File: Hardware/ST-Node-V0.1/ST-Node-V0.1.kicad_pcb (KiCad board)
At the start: 2 copper layers, 40.9 x 67.7 mm, 149 parts, among them J1 U.FL-R-SMT-1, Q1 SI2323DS, Q2 2SC4213, SW1 RESET, SW2 SW_Push, U1 TPS22917DBV, U10 LIS2DH12, U11 SHTC3, U12 ATECC608A-TNGLORAU, U2 RP605Z283B, U3 TPS22917DBV, U4 TPS22917DBV, U5 STM32WLxx_QFN48, U6 NX3L1T3157GM, U7 BGS13S4N9, U8 NX3L1T3157GM, U9 MX25R1635, X1 32MHz, X2 32.768KHz

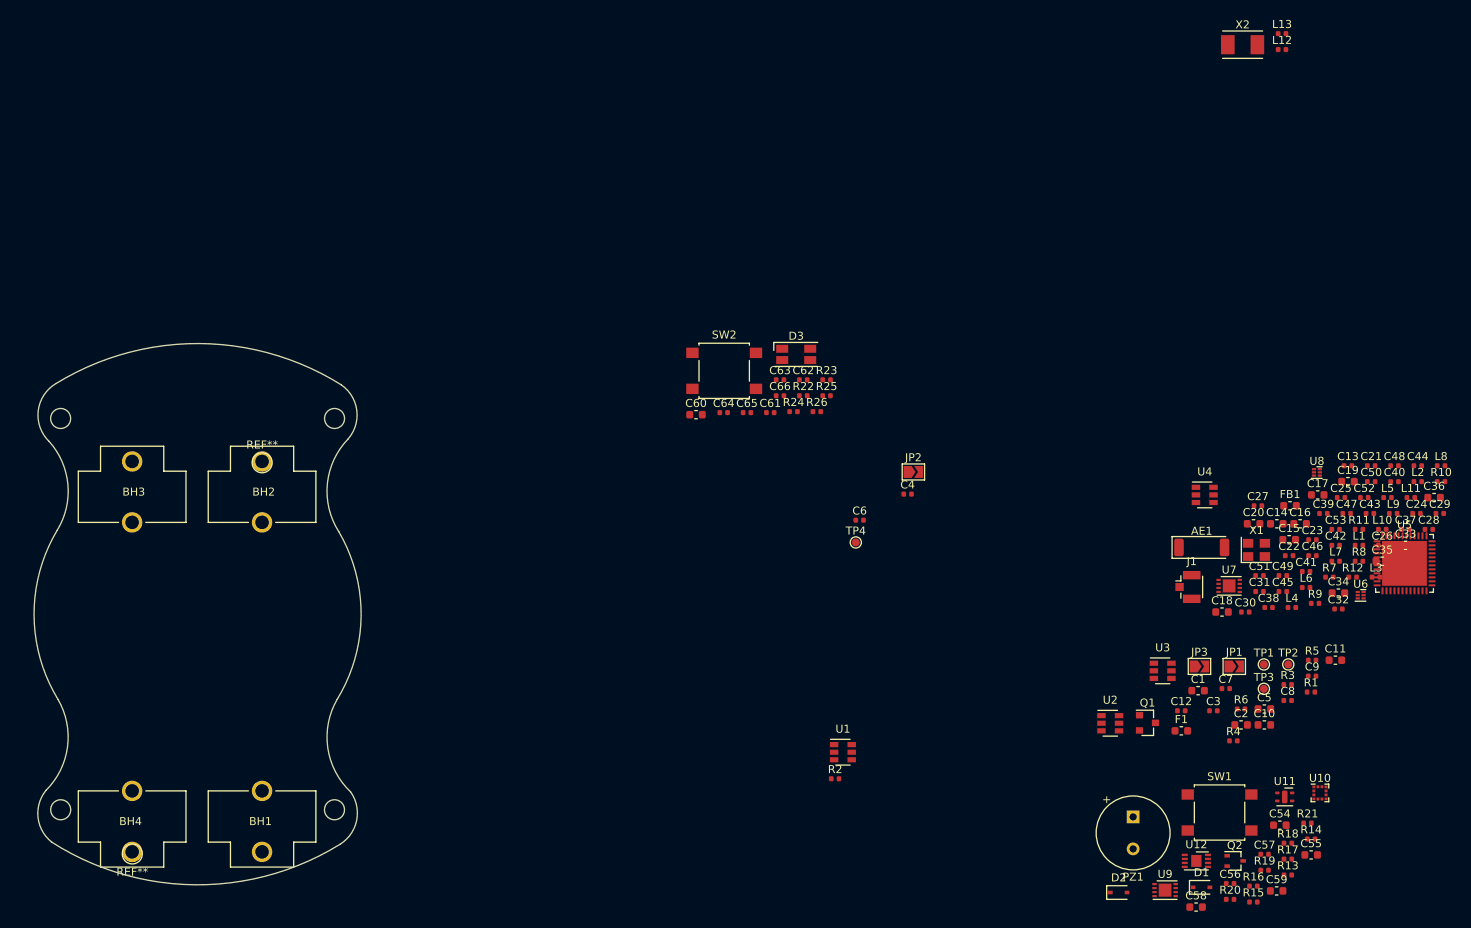
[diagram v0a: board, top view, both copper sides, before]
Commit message: sch:  Swap couple of pins and fix a HW bug
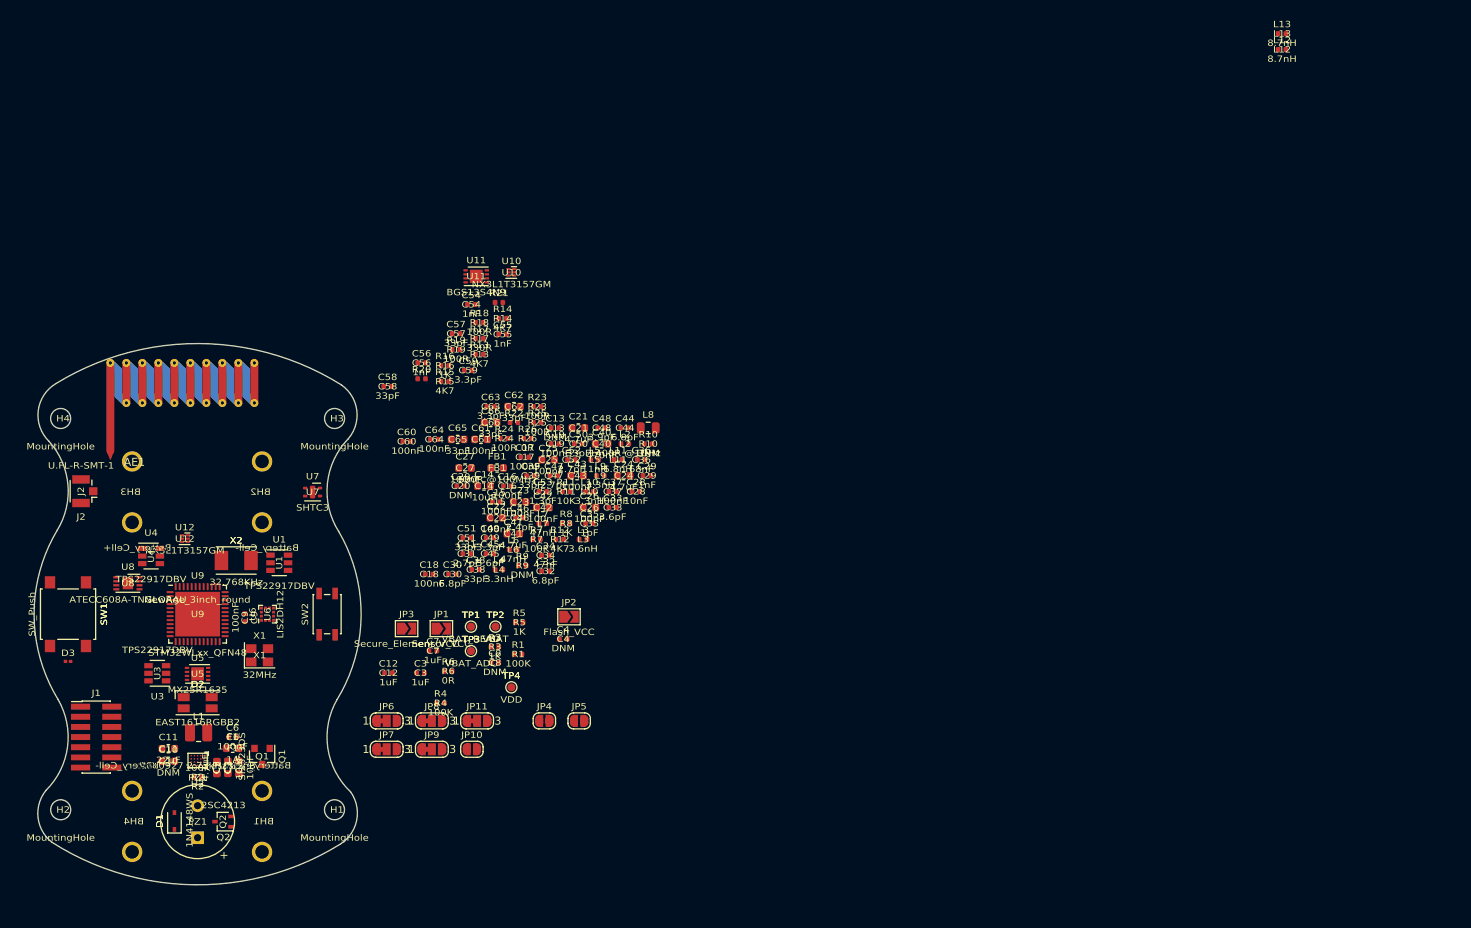
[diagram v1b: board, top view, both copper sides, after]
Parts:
- removed REF** (x2): Pin_D1.0mm_L10.0mm, Connector_Pin:Pin_D1.0mm_L10.0mm
- added J2: U.FL-R-SMT-1, Connector_Coaxial:U.FL_Hirose_U.FL-R-SMT-1_Vertical, F.Cu at (125.6, 83.7)
- added JP10: BOOT0, Jumper:SolderJumper-2_P1.3mm_Open_RoundedPad1.0x1.5mm, F.Cu at (174.0, 116.0)
- added JP11: VDD_RF_SW, Jumper:SolderJumper-3_P1.3mm_Bridged12_RoundedPad1.0x1.5mm_NumberLabels, F.Cu at (174.6, 112.4)
- added JP4: SDA, Jumper:SolderJumper-2_P1.3mm_Open_RoundedPad1.0x1.5mm, F.Cu at (183.0, 112.4)
- added JP5: SCL, Jumper:SolderJumper-2_P1.3mm_Open_RoundedPad1.0x1.5mm, F.Cu at (187.4, 112.4)
- added JP6: JTDI, Jumper:SolderJumper-3_P1.3mm_Bridged12_RoundedPad1.0x1.5mm_NumberLabels, F.Cu at (163.3, 112.4)
- added JP7: VBAT, Jumper:SolderJumper-3_P1.3mm_Bridged12_RoundedPad1.0x1.5mm_NumberLabels, F.Cu at (163.3, 116.0)
- added JP8: SWO, Jumper:SolderJumper-3_P1.3mm_Bridged12_RoundedPad1.0x1.5mm_NumberLabels, F.Cu at (169.0, 112.4)
- added JP9: PB12, Jumper:SolderJumper-3_P1.3mm_Bridged12_RoundedPad1.0x1.5mm_NumberLabels, F.Cu at (169.0, 116.0)
- AE1: value Dual_Band_868/915 -> Antenna; footprint RF_Antenna:Johanson_2450AT43F0100 -> RF_Antenna:Texas_SWRA416_868MHz_915MHz
- BH1, BH2, BH3, BH4: moved to B.Cu
- C14: value 4.7uF -> 10uF
- C15, C16, C18, C19, C58: footprint Capacitor_SMD:C_0603_1608Metric -> Capacitor_SMD:C_0402_1005Metric
- C17: value 4.7uF -> 100nF; footprint Capacitor_SMD:C_0603_1608Metric -> Capacitor_SMD:C_0402_1005Metric
- C20: value 100nF -> DNM; footprint Capacitor_SMD:C_0603_1608Metric -> Capacitor_SMD:C_0402_1005Metric
- C21: value 10nF -> 4.7uF; footprint Capacitor_SMD:C_0402_1005Metric -> Capacitor_SMD:C_0603_1608Metric
- C22: value 1nF -> 100nF; footprint Capacitor_SMD:C_0402_1005Metric -> Capacitor_SMD:C_0603_1608Metric
- C23, C25: value 6.8pF -> 100nF; footprint Capacitor_SMD:C_0402_1005Metric -> Capacitor_SMD:C_0603_1608Metric
- C24: value 2.7pF -> 4.7uF; footprint Capacitor_SMD:C_0402_1005Metric -> Capacitor_SMD:C_0603_1608Metric
- C26: value 3.6pF -> 100nF; footprint Capacitor_SMD:C_0402_1005Metric -> Capacitor_SMD:C_0603_1608Metric
- C27: value 47nF -> 100nF; footprint Capacitor_SMD:C_0402_1005Metric -> Capacitor_SMD:C_0603_1608Metric
- C28: value 1pF -> 10nF
- C29: value 68nF -> 1nF
- C30: value 100nF -> 6.8pF
- C31: value 33pF -> 2.7pF
- C32, C44: value 33pF -> 6.8pF
- C33: value 470nF -> 3.6pF; footprint Capacitor_SMD:C_0603_1608Metric -> Capacitor_SMD:C_0402_1005Metric
- C34: value 4.7uF -> 47nF; footprint Capacitor_SMD:C_0603_1608Metric -> Capacitor_SMD:C_0402_1005Metric
- C35: value 100nF -> 1pF; footprint Capacitor_SMD:C_0603_1608Metric -> Capacitor_SMD:C_0402_1005Metric
- C36: value 100nF -> 68nF; footprint Capacitor_SMD:C_0603_1608Metric -> Capacitor_SMD:C_0402_1005Metric
- C37: value 6.8pF -> 100nF
- C38: value 5.6pF -> 33pF
- C39: value 2.4pF -> 33pF
- C40: value 2.7pF -> 470nF; footprint Capacitor_SMD:C_0402_1005Metric -> Capacitor_SMD:C_0603_1608Metric
- C41: value 3.9pF -> 4.7uF; footprint Capacitor_SMD:C_0402_1005Metric -> Capacitor_SMD:C_0603_1608Metric
- C42: value 3.3pF -> 100nF; footprint Capacitor_SMD:C_0402_1005Metric -> Capacitor_SMD:C_0603_1608Metric
- C43: value 33pF -> 100nF; footprint Capacitor_SMD:C_0402_1005Metric -> Capacitor_SMD:C_0603_1608Metric
- C45: value 2.7pF -> 5.6pF
- C46: value 1.3pF -> 2.4pF
- C47: value 1nF -> 2.7pF
- C48: value 1nF -> 3.9pF
- C49: value 1nF -> 3.3pF
- C52: value 3.3pF -> 2.7pF
- C53: value 100nF -> 1.3pF
- C54: value 100nF -> 1nF; footprint Capacitor_SMD:C_0603_1608Metric -> Capacitor_SMD:C_0402_1005Metric
- C55: value 33pF -> 1nF; footprint Capacitor_SMD:C_0603_1608Metric -> Capacitor_SMD:C_0402_1005Metric
- C56: value 3.3pF -> 1nF
- C57: value 100nF -> 33pF
- C59: value 33pF -> 3.3pF; footprint Capacitor_SMD:C_0603_1608Metric -> Capacitor_SMD:C_0402_1005Metric
- C60: value 10uF -> 100nF; footprint Capacitor_SMD:C_0603_1608Metric -> Capacitor_SMD:C_0402_1005Metric
- C61: footprint Capacitor_SMD:C_0402_1005Metric -> Capacitor_SMD:C_0603_1608Metric
- C62, C65, C66: value 100nF -> 33pF; footprint Capacitor_SMD:C_0402_1005Metric -> Capacitor_SMD:C_0603_1608Metric
- C63: value 100nF -> 3.3pF
- D1: value ESDALC6V1-1U2 -> 1N4148WS
- D2: value 1N4148WS -> EAST1616RGBB2; footprint Diode_SMD:D_SOD-323 -> LED_SMD:LED_RGB_1210
- D3: value EAST1616RGBB2 -> ESDALC6V1-1U2; footprint LED_SMD:LED_RGB_1210 -> Inductor_SMD:L_0201_0603Metric
- J1: value U.FL-R-SMT-1 -> Debug; footprint Connector_Coaxial:U.FL_Hirose_U.FL-R-SMT-1_Vertical -> Connector_PinHeader_1.27mm:PinHeader_2x07_P1.27mm_Vertical_SMD
- L1: footprint Inductor_SMD:L_0402_1005Metric -> Inductor_SMD:L_1008_2520Metric
- L8: footprint Inductor_SMD:L_0402_1005Metric -> Inductor_SMD:L_0805_2012Metric
- R10: value 220R -> DNM
- R12, R13, R14: value 100R -> 4K7
- R15: value 0R -> 4K7
- R16: value DNM -> 1K
- R17: value DNM -> 330R
- R18: value 10K -> 100R
- R19: value 4K7 -> 100R
- R20, R22: value 4K7 -> 10K; footprint Resistor_SMD:R_0402_1005Metric -> Inductor_SMD:L_0402_1005Metric
- R21: value 4K7 -> 220R; footprint Resistor_SMD:R_0402_1005Metric -> Inductor_SMD:L_0402_1005Metric
- R23: value 1K -> 100R
- R24: value 330R -> 100R
- R26: value 100R -> 0R
- R9: value 10K -> DNM
- SW1: value RESET -> SW_Push
- SW2: value SW_Push -> RESET; footprint Button_Switch_SMD:SW_SPST_B3S-1000 -> Button_Switch_SMD:SW_SPST_EVQP2
- U10: value LIS2DH12 -> NX3L1T3157GM; footprint Package_LGA:LGA-12_2x2mm_P0.5mm -> Package_DFN_QFN:DFN-6_1.3x1.2mm_P0.4mm
- U11: value SHTC3 -> BGS13S4N9; footprint Sensor_Humidity:Sensirion_DFN-4-1EP_2x2mm_P1mm_EP0.7x1.6mm -> Package_CSP:LFCSP-8-1EP_3x2mm_P0.5mm_EP1.6x1.65mm
- U12: value ATECC608A-TNGLORAU -> NX3L1T3157GM; footprint Package_DFN_QFN:DFN-8-1EP_3x2mm_P0.5mm_EP1.3x1.5mm -> Package_DFN_QFN:DFN-6_1.3x1.2mm_P0.4mm
- U2: footprint Package_TO_SOT_SMD:SOT-23-6 -> node-lib-v1:WLCSP-20-P3_1.994x1.609mm_Layout5x4_P0.4mm
- U5: value STM32WLxx_QFN48 -> MX25R1635; footprint Package_DFN_QFN:QFN-48-1EP_7x7mm_P0.5mm_EP5.6x5.6mm -> Package_CSP:LFCSP-8-1EP_3x2mm_P0.5mm_EP1.6x1.65mm
- U6: value NX3L1T3157GM -> LIS2DH12; footprint Package_DFN_QFN:DFN-6_1.3x1.2mm_P0.4mm -> Package_LGA:LGA-12_2x2mm_P0.5mm
- U7: value BGS13S4N9 -> SHTC3; footprint Package_CSP:LFCSP-8-1EP_3x2mm_P0.5mm_EP1.6x1.65mm -> Sensor_Humidity:Sensirion_DFN-4-1EP_2x2mm_P1mm_EP0.7x1.6mm
- U8: value NX3L1T3157GM -> ATECC608A-TNGLORAU; footprint Package_DFN_QFN:DFN-6_1.3x1.2mm_P0.4mm -> Package_DFN_QFN:DFN-8-1EP_3x2mm_P0.5mm_EP1.3x1.5mm
- U9: value MX25R1635 -> STM32WLxx_QFN48; footprint Package_CSP:LFCSP-8-1EP_3x2mm_P0.5mm_EP1.6x1.65mm -> Package_DFN_QFN:QFN-48-1EP_7x7mm_P0.5mm_EP5.6x5.6mm
- moved U5 151.5 mm to (139.7, 106.5)
- moved U8 149.3 mm to (131.0, 95.2)
- moved L1 146.9 mm to (139.8, 113.9)
- moved C11 146.3 mm to (136.0, 115.9)
- moved SW1 146.1 mm to (123.5, 99.1), turned to 270 degrees
- moved X2 141.4 mm to (144.5, 92.4)
- moved J1 137.8 mm to (127.0, 114.4)
- moved C10 137.1 mm to (136.0, 117.4)
- moved U6 136.7 mm to (148.4, 99.1), turned to 90 degrees
- moved C9 133.6 mm to (145.6, 99.5), turned to 270 degrees
- moved U12 132.7 mm to (138.1, 89.6)
- moved U4 131.9 mm to (133.9, 91.8)
- moved C5 131.1 mm to (142.1, 118.2), turned to 270 degrees
- moved D1 128.6 mm to (136.8, 124.9), turned to 90 degrees
- moved AE1 128.6 mm to (137.8, 73.5)
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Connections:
- C14 pad 1: VDD -> GND
- C14 pad 2: GND -> /Power Supply/VCC_SEC_ELM
- C15 pad 1: VDD -> GND
- C15 pad 2: GND -> /Power Supply/VCC_SEC_ELM
- C16 pad 1: Net-(C16-Pad1) -> GND
- C16 pad 2: GND -> /Peripherals/VCC_FLASH
- C17 pad 1: VDDA -> GND
- C17 pad 2: GND -> /Power Supply/VCC_SEC_ELM
- C18 pad 1: VDD -> GND
- C18 pad 2: GND -> /Peripherals/VCC_SEC_ELM
- C19 pad 1: VDDA -> GND
- C19 pad 2: GND -> /Power Supply/VCC_SEC_ELM
- C20 pad 1: VDD -> GND
- C20 pad 2: GND -> /LoRa MCU/PB3
- C21 pad 1: GND -> VDD
- C21 pad 2: Net-(C21-Pad2) -> GND
- C22 pad 1: Net-(C22-Pad1) -> VDD
- C22 pad 2: OSC_IN -> GND
- C23 pad 1: GND -> Net-(C23-Pad1)
- C23 pad 2: OSC32_IN -> GND
- C24 pad 1: GND -> VDDA
- C24 pad 2: Net-(C24-Pad2) -> GND
- C25 pad 1: GND -> VDD
- C25 pad 2: OSC32_OUT -> GND
- C26 pad 1: Net-(C26-Pad1) -> VDDA
- C26 pad 2: Net-(C26-Pad2) -> GND
- C27 pad 1: GND -> VDD
- C27 pad 2: Net-(C27-Pad2) -> GND
- C28 pad 1: Net-(C26-Pad2) -> GND
- C28 pad 2: GND -> Net-(C28-Pad2)
- C29 pad 1: Net-(C27-Pad2) -> Net-(C29-Pad1)
- C29 pad 2: GND -> OSC_IN
- C30 pad 2: NRST -> OSC32_IN
- C32 pad 1: Net-(C32-Pad1) -> GND
- C32 pad 2: GND -> OSC32_OUT
- C33 pad 1: VDDRF1V55 -> Net-(C33-Pad1)
- C33 pad 2: GND -> Net-(C33-Pad2)
- C34 pad 1: VDDRF -> GND
- C34 pad 2: GND -> Net-(C34-Pad2)
- C35 pad 1: VDDRF1V55 -> Net-(C33-Pad2)
- C36 pad 1: VDDRF -> Net-(C34-Pad2)
- C37 pad 2: Net-(C37-Pad2) -> NRST
- C39 pad 1: Net-(C37-Pad2) -> Net-(C39-Pad1)
- C39 pad 2: Net-(C39-Pad2) -> GND
- C40 pad 1: Net-(C38-Pad2) -> VDDRF1V55
- C40 pad 2: Net-(C40-Pad2) -> GND
- C41 pad 1: GND -> VDDRF
- C41 pad 2: Net-(C39-Pad2) -> GND
- C42 pad 1: GND -> VDDRF1V55
- C42 pad 2: Net-(C40-Pad2) -> GND
- C43 pad 1: Net-(C39-Pad2) -> VDDRF
- C43 pad 2: Net-(C43-Pad2) -> GND
- C44 pad 1: Net-(C40-Pad2) -> GND
- C46 pad 1: GND -> Net-(C44-Pad2)
- C47 pad 1: GND -> Net-(C45-Pad2)
- C48 pad 2: Net-(C48-Pad2) -> Net-(C46-Pad2)
- C49 pad 2: Net-(C49-Pad2) -> Net-(C47-Pad2)
- C50 pad 1: Net-(C50-Pad1) -> Net-(C46-Pad2)
- C51 pad 1: Net-(C50-Pad1) -> Net-(C47-Pad2)
- C52 pad 2: Net-(C50-Pad2) -> Net-(C52-Pad2)
- C53 pad 2: Net-(C51-Pad2) -> Net-(C53-Pad2)
- C54 pad 1: PB0_VDD_TCXO -> GND
- C54 pad 2: GND -> Net-(C54-Pad2)
- C55 pad 1: VDDRF1V55 -> GND
- C55 pad 2: GND -> Net-(C55-Pad2)
- C56 pad 2: Net-(AE1-Pad1) -> Net-(C56-Pad2)
- C57 pad 1: GND -> Net-(C57-Pad1)
- C58 pad 1: VDDRF -> Net-(C57-Pad1)
- C58 pad 2: GND -> Net-(C58-Pad2)
- C59 pad 1: VDDPA -> GND
- C59 pad 2: GND -> Net-(C57-Pad2)
- C60 pad 2: /Peripherals/VCC_SENSORS -> Net-(C58-Pad2)
- C61 pad 1: GND -> PB0_VDD_TCXO
- C61 pad 2: /Peripherals/VCC_SENSORS -> GND
- C62 pad 1: GND -> VDDRF1V55
- C62 pad 2: /Peripherals/VCC_FLASH -> GND
- C63 pad 2: /Peripherals/VCC_SENSORS -> Net-(AE1-Pad1)
- C64 pad 2: /Peripherals/VCC_SEC_ELM -> Net-(C64-Pad2)
- C65 pad 1: GND -> VDDRF
- C65 pad 2: /Peripherals/VCC_SENSOR -> GND
- C66 pad 1: GND -> VDDPA
- C66 pad 2: /Peripherals/USR_BTN -> GND
- C9 pad 1: /Power Supply/VBAT_ADC -> /LoRa MCU/PB2
- D1 pad 1: NRST -> VDD
- D1 pad 2: GND -> Net-(D1-Pad2)
- D2 pad 1: VDD -> Net-(D2-Pad1)
- D3 pad 1: Net-(D3-Pad1) -> NRST
- D3 pad 2: Net-(D3-Pad2) -> GND
- J1 pad 1: Net-(C57-Pad2) -> Net-(J1-Pad1)
- J1 pad 2: GND -> Net-(J1-Pad2)
- JP1 pad 2: /Peripherals/VCC_SENSORS -> /Peripherals/VCC_SEC_ELM
- JP3 pad 2: /Peripherals/VCC_SEC_ELM -> /Power Supply/VCC_SEC_ELM
- L1 pad 1: (no net) -> Net-(L1-Pad1)
- L1 pad 2: (no net) -> Net-(L1-Pad2)
- L10 pad 1: Net-(C38-Pad2) -> Net-(C45-Pad2)
- L10 pad 2: Net-(C40-Pad2) -> Net-(C47-Pad2)
- L11 pad 1: Net-(C43-Pad2) -> Net-(C50-Pad2)
- L11 pad 2: Net-(C45-Pad2) -> Net-(C52-Pad2)
- L12 pad 1: Net-(C44-Pad2) -> Net-(C51-Pad2)
- L12 pad 2: Net-(C46-Pad2) -> Net-(C53-Pad2)
- L13 pad 1: Net-(C50-Pad2) -> Net-(C57-Pad2)
- L2 pad 2: Net-(C21-Pad2) -> Net-(C28-Pad2)
- L3 pad 2: Net-(C37-Pad2) -> Net-(C44-Pad2)
- L4 pad 2: Net-(C38-Pad2) -> Net-(C45-Pad2)
- L5 pad 1: Net-(C24-Pad2) -> Net-(C31-Pad2)
- L5 pad 2: Net-(C26-Pad1) -> Net-(C33-Pad1)
- L6 pad 1: Net-(C32-Pad1) -> Net-(C39-Pad1)
- L6 pad 2: Net-(C38-Pad2) -> Net-(C45-Pad2)
- L7 pad 1: Net-(C31-Pad2) -> Net-(C38-Pad2)
- L7 pad 2: Net-(C37-Pad2) -> Net-(C44-Pad2)
- L9 pad 1: Net-(C37-Pad2) -> Net-(C44-Pad2)
- L9 pad 2: Net-(C39-Pad2) -> Net-(C46-Pad2)
- PZ1 pad 2: Net-(D2-Pad2) -> Net-(D1-Pad2)
- Q2 pad 3: Net-(D2-Pad2) -> Net-(D1-Pad2)
- R1 pad 2: /Power Supply/VCC_SENSOR_EN -> /LoRa MCU/PB7
- R10 pad 1: Net-(C22-Pad1) -> /Peripherals/VCC_FLASH
- R11 pad 1: GND -> /Peripherals/VCC_FLASH
- R11 pad 2: (no net) -> Net-(R11-Pad2)
- R12 pad 1: Net-(C47-Pad2) -> /LoRa MCU/I2C1_SDA
- R12 pad 2: FE_CTRL1 -> /Power Supply/VCC_SEC_ELM
- R13 pad 1: Net-(C48-Pad2) -> /Power Supply/VCC_SEC_ELM
- R13 pad 2: FE_CTRL2 -> /LoRa MCU/I2C1_SCL
- R14 pad 1: (no net) -> /LoRa MCU/I2C2_SCL
- R14 pad 2: Net-(C49-Pad2) -> /Peripherals/VCC_SEC_ELM
- R15 pad 1: Net-(C57-Pad2) -> /Peripherals/VCC_SEC_ELM
- R15 pad 2: Net-(C51-Pad2) -> /LoRa MCU/I2C2_SDA
- R16 pad 1: /Peripherals/VCC_FLASH -> /Peripherals/BUZZER
- R16 pad 2: Net-(R16-Pad2) -> Net-(Q2-Pad1)
- R17 pad 1: /Peripherals/VCC_FLASH -> Net-(D2-Pad1)
- R17 pad 2: Net-(R17-Pad2) -> /Peripherals/LED_R
- R18 pad 1: /Peripherals/VCC_FLASH -> Net-(D2-Pad2)
- R18 pad 2: Net-(R18-Pad2) -> /Peripherals/LED_G
- R19 pad 1: /Peripherals/SDA -> Net-(D2-Pad3)
- R19 pad 2: /Peripherals/VCC_SENSORS -> /Peripherals/LED_B
- R2 pad 2: /Power Supply/VBAT_READ -> /LoRa MCU/PB4
- R20 pad 1: /Peripherals/VCC_SENSORS -> OSC_IN
- R20 pad 2: /Peripherals/SCL -> GND
- R21 pad 1: /Peripherals/SEC_ELM_SCL -> Net-(C29-Pad1)
- R21 pad 2: /Peripherals/VCC_SEC_ELM -> Net-(R21-Pad2)
- R22 pad 1: /Peripherals/VCC_SEC_ELM -> GND
- R22 pad 2: /Peripherals/SEC_ELM_SDA -> Net-(JP10-Pad2)
- R23 pad 1: (no net) -> Net-(C54-Pad2)
- R23 pad 2: Net-(Q2-Pad1) -> FE_CTRL1
- R24 pad 1: Net-(D3-Pad1) -> Net-(C55-Pad2)
- R24 pad 2: (no net) -> FE_CTRL2
- R25 pad 1: Net-(D3-Pad2) -> Net-(JP11-Pad2)
- R25 pad 2: (no net) -> Net-(C56-Pad2)
- R26 pad 1: Net-(D3-Pad3) -> Net-(C64-Pad2)
- R26 pad 2: (no net) -> Net-(C58-Pad2)
- R3 pad 1: /Peripherals/VCC_SENSORS -> /Peripherals/VCC_SEC_ELM
- R4 pad 2: /Power Supply/VCC_FLASH_EN -> /LoRa MCU/PB5
- R7 pad 2: /Power Supply/VCC_SEC_ELM_EN -> /LoRa MCU/PB6
- R8 pad 1: /Peripherals/VCC_SEC_ELM -> /Power Supply/VCC_SEC_ELM
- R9 pad 1: OSC_IN -> /Peripherals/VCC_FLASH
- R9 pad 2: GND -> Net-(R9-Pad2)
- SW1 pad 2: NRST -> /LoRa MCU/PB3
- SW2 pad 2: /Peripherals/USR_BTN -> NRST
- TP1 pad 1: /Power Supply/VBAT_READ -> /LoRa MCU/PB4
- TP3 pad 1: /Power Supply/VBAT_ADC -> /LoRa MCU/PB2
- U1 pad 3: /Power Supply/VCC_SENSOR_EN -> /LoRa MCU/PB7
- U1 pad 6: /Peripherals/VCC_SENSORS -> /Peripherals/VCC_SEC_ELM
- U10 pad 1: /Peripherals/SCL -> Net-(C39-Pad1)
- U10 pad 2: /Peripherals/VCC_SENSORS -> GND
- U10 pad 3: /Peripherals/VCC_SENSORS -> Net-(C38-Pad2)
- U10 pad 4: /Peripherals/SDA -> Net-(C34-Pad2)
- U10 pad 5: GND -> VDD
- U10 pad 6: GND -> FE_CTRL1
- U11 pad 1: /Peripherals/VCC_SENSOR -> Net-(C54-Pad2)
- U11 pad 2: /Peripherals/SCL -> Net-(C53-Pad2)
- U11 pad 3: /Peripherals/SDA -> Net-(C33-Pad2)
- U11 pad 4: GND -> Net-(C57-Pad1)
- U11 pad 5: (no net) -> Net-(C52-Pad2)
- U12 pad 1: (no net) -> VDDRF1V55
- U12 pad 2: (no net) -> GND
- U12 pad 3: (no net) -> VDDRF
- U12 pad 4: GND -> VDDPA
- U12 pad 5: /Peripherals/SEC_ELM_SDA -> VDD
- U12 pad 6: /Peripherals/SEC_ELM_SCL -> FE_CTRL1
- U3 pad 3: /Power Supply/VCC_FLASH_EN -> /LoRa MCU/PB5
- U4 pad 3: /Power Supply/VCC_SEC_ELM_EN -> /LoRa MCU/PB6
- U4 pad 6: /Peripherals/VCC_SEC_ELM -> /Power Supply/VCC_SEC_ELM
- U5 pad 1: (no net) -> Net-(R11-Pad2)
- U5 pad 2: FE_CTRL1 -> /Peripherals/MISO
- U5 pad 3: FE_CTRL2 -> Net-(R10-Pad2)
- U5 pad 4: (no net) -> GND
- U5 pad 5: (no net) -> /Peripherals/MOSI
- U5 pad 6: (no net) -> /Peripherals/SCLK
- U5 pad 7: (no net) -> Net-(R9-Pad2)
- U5 pad 8: (no net) -> /Peripherals/VCC_FLASH
- U5 pad 9: (no net) -> GND
- U6 pad 1: Net-(C32-Pad1) -> /LoRa MCU/I2C1_SCL
- U6 pad 2: GND -> /Power Supply/VCC_SEC_ELM
- U6 pad 3: Net-(C31-Pad2) -> /Power Supply/VCC_SEC_ELM
- U6 pad 4: Net-(C27-Pad2) -> /LoRa MCU/I2C1_SDA
- U6 pad 5: VDD -> GND
- U6 pad 6: FE_CTRL1 -> GND
- U7 pad 1: Net-(C47-Pad2) -> /Power Supply/VCC_SEC_ELM
- U7 pad 2: Net-(C46-Pad2) -> /LoRa MCU/I2C1_SCL
- U7 pad 3: Net-(C26-Pad2) -> /LoRa MCU/I2C1_SDA
- U7 pad 4: Net-(C50-Pad1) -> GND
- U7 pad 5: Net-(C45-Pad2) -> (no net)
- U8 pad 1: VDDRF1V55 -> (no net)
- U8 pad 2: GND -> (no net)
- U8 pad 3: VDDRF -> (no net)
- U8 pad 4: VDDPA -> GND
- U8 pad 5: VDD -> /LoRa MCU/I2C2_SDA
- U8 pad 6: FE_CTRL1 -> /LoRa MCU/I2C2_SCL
- U9 pad 1: Net-(R18-Pad2) -> Net-(JP8-Pad2)
- U9 pad 2: (no net) -> /LoRa MCU/PB4
- U9 pad 3: Net-(R17-Pad2) -> /LoRa MCU/PB5
- U9 pad 4: GND -> /LoRa MCU/PB6
- U9 pad 5: (no net) -> /LoRa MCU/PB7
- U9 pad 6: (no net) -> /Peripherals/LED_B
- U9 pad 7: Net-(R16-Pad2) -> FE_CTRL1
- U9 pad 8: /Peripherals/VCC_FLASH -> FE_CTRL2
- U9 pad 9: GND -> /LoRa MCU/USART2_TxD
- X1 pad 3: Net-(R10-Pad2) -> Net-(R21-Pad2)
- X1 pad 4: Net-(C21-Pad2) -> Net-(C28-Pad2)

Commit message: sch, pcb: Improve pcb layout, swap sch pins
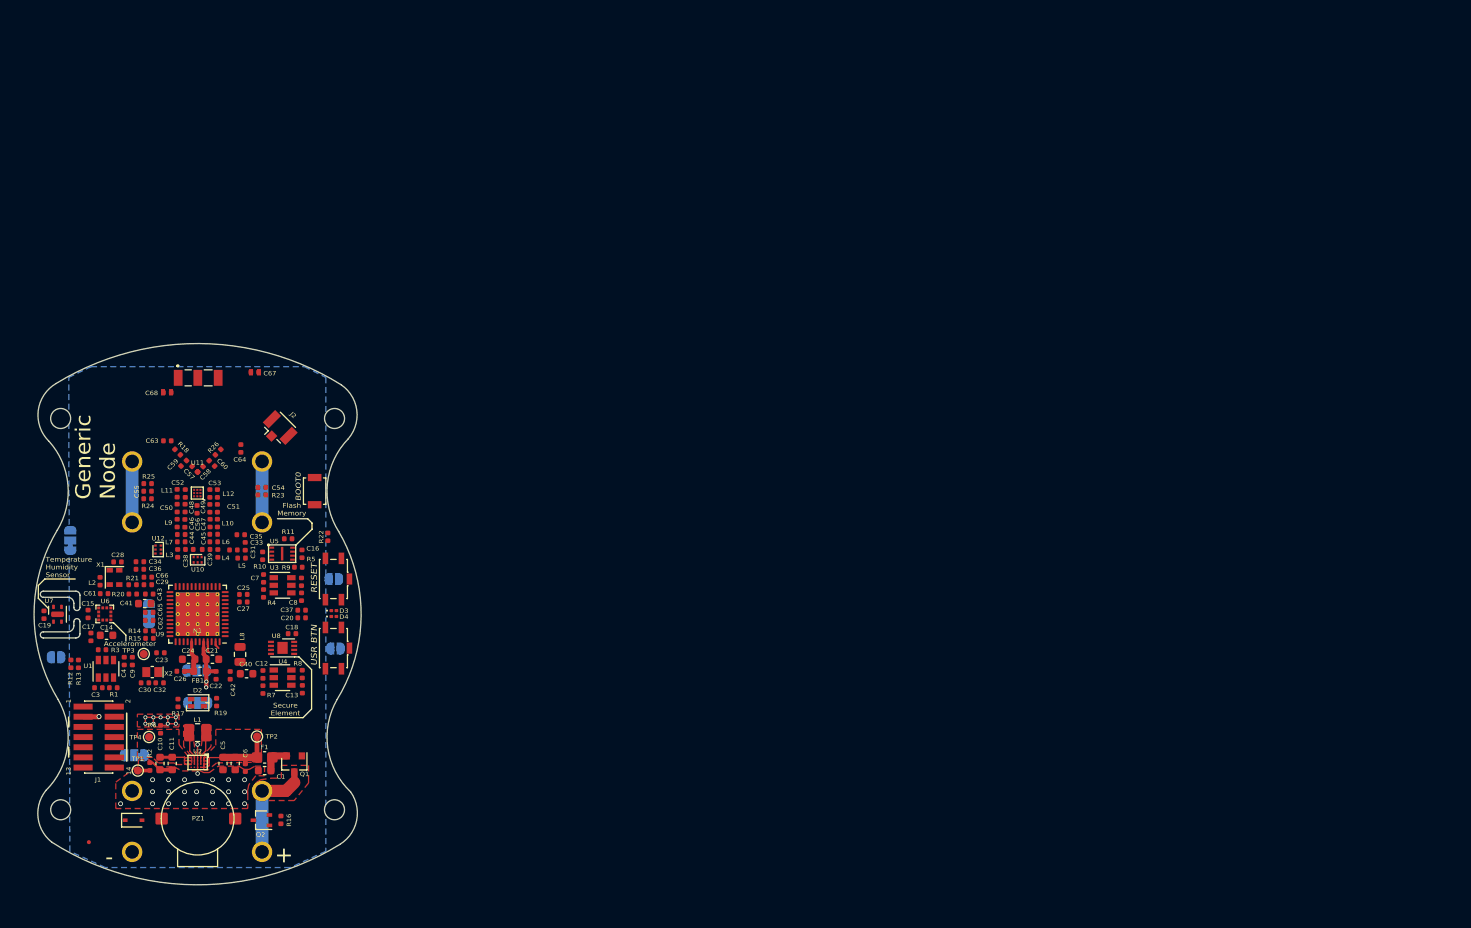
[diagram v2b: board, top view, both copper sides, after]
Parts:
- removed JP4: SDA, Jumper:SolderJumper-2_P1.3mm_Open_RoundedPad1.0x1.5mm
- removed JP5: SCL, Jumper:SolderJumper-2_P1.3mm_Open_RoundedPad1.0x1.5mm
- removed L13: 8.7nH, Inductor_SMD:L_0402_1005Metric
- added C67: 5.0pF, Capacitor_SMD:C_0402_1005Metric, F.Cu at (146.8, 68.8)
- added C68: 3.6pF, Capacitor_SMD:C_0402_1005Metric, F.Cu at (135.9, 71.4)
- added D4: ESDALC6V1-1U2, Diode_SMD:D_0201_0603Metric, F.Cu at (156.7, 99.4)
- added FID1: Fiducial, Fiducial:Fiducial_0.5mm_Mask1.5mm, F.Cu at (126.1, 127.6)
- AE1: value Antenna -> ANT_M620720; footprint RF_Antenna:Texas_SWRA416_868MHz_915MHz -> node-lib-v1:ANT_M620720
- C22, C23, C25, C26, C27, C42, C43, C61, C62, C65, C66: footprint Capacitor_SMD:C_0603_1608Metric -> Capacitor_SMD:C_0402_1005Metric
- C35: value 1pF -> DNM
- C58: value 33pF -> DNM
- C59, C63: value 3.3pF -> DNM
- C60, C64: value 100nF -> DNM
- D2: footprint LED_SMD:LED_RGB_1210 -> node-lib-v1:LED_RGB_0606
- D3: footprint Inductor_SMD:L_0201_0603Metric -> Diode_SMD:D_0201_0603Metric
- F1: value 1A -> PTC 6V 750MA; footprint Fuse:Fuse_0603_1608Metric -> node-lib-v1:Fuse_0805_2012Metric_Castellated
- J1: footprint Connector_PinHeader_1.27mm:PinHeader_2x07_P1.27mm_Vertical_SMD -> node-lib-v1:PinHeader_2x07_P1.27mm_Vertical_SMD
- JP1, JP2, JP3: footprint Jumper:SolderJumper-2_P1.3mm_Open_TrianglePad1.0x1.5mm -> Jumper:SolderJumper-2_P1.3mm_Open_RoundedPad1.0x1.5mm; moved to B.Cu
- JP10: footprint Jumper:SolderJumper-2_P1.3mm_Open_RoundedPad1.0x1.5mm -> Button_Switch_SMD:SW_SPST_B3U-1000P
- JP11, JP6, JP7, JP8: moved to B.Cu
- JP9: value PB12 -> INT; moved to B.Cu
- PZ1: footprint Buzzer_Beeper:MagneticBuzzer_CUI_CST-931RP-A -> node-lib-v1:Buzzer_AST0927MW-3.6TRQ
- R18: value 100R -> 0R
- R20: value 10K -> DNM
- SW1: footprint Button_Switch_SMD:SW_SPST_B3S-1000 -> node-lib-v1:EVQ-P2R02W
- SW2: footprint Button_Switch_SMD:SW_SPST_EVQP2 -> node-lib-v1:EVQ-P2R02W
- U10, U12: footprint Package_DFN_QFN:DFN-6_1.3x1.2mm_P0.4mm -> node-lib-v1:6-XFDFN_SOT-886
- U11: footprint Package_CSP:LFCSP-8-1EP_3x2mm_P0.5mm_EP1.6x1.65mm -> node-lib-v1:RFSW_BGS13S4N9E6327XTSA1
- U5: footprint Package_CSP:LFCSP-8-1EP_3x2mm_P0.5mm_EP1.6x1.65mm -> node-lib-v1:FLASH_UFDFN-8-MX25R1635F
- U7: footprint Sensor_Humidity:Sensirion_DFN-4-1EP_2x2mm_P1mm_EP0.7x1.6mm -> node-lib-v1:Sensirion_DFN-4-1EP_2x2mm_P1mm_EP0.7x1.6mm
- U9: footprint Package_DFN_QFN:QFN-48-1EP_7x7mm_P0.5mm_EP5.6x5.6mm -> Package_DFN_QFN:QFN-48-1EP_7x7mm_P0.5mm_EP5.45x5.45mm_ThermalVias
- X1: footprint Oscillator:Oscillator_SMD_Abracon_ASE-4Pin_3.2x2.5mm -> node-lib-v1:TCXO_NT2016SA-32M-END4263A
- X2: footprint Crystal:Crystal_SMD_TXC_7A-2Pin_5x3.2mm -> node-lib-v1:Crystal_SMD_NX2012SA_32.768KHz
- moved L12 144.2 mm to (142.2, 84.0), turned to 90 degrees
- moved L2 67.8 mm to (127.5, 94.9), turned to 90 degrees
- moved C19 67.4 mm to (120.5, 99.1), turned to 270 degrees
- moved C28 65.4 mm to (129.7, 92.5)
- moved C36 64.1 mm to (132.5, 93.4), turned to 180 degrees
- moved C29 63.9 mm to (133.5, 95.4)
- moved R13 63.3 mm to (124.8, 105.3), turned to 270 degrees
- moved R12 63.1 mm to (123.9, 105.3), turned to 90 degrees
- moved R16 60.4 mm to (150.1, 124.8), turned to 270 degrees
- moved R17 59.1 mm to (137.2, 110.2), turned to 90 degrees
- moved C24 59.0 mm to (138.6, 104.7), turned to 180 degrees
- moved R14 58.9 mm to (133.7, 101.1), turned to 180 degrees
- moved C17 58.7 mm to (126.4, 101.9), turned to 90 degrees
- moved L8 58.3 mm to (145.0, 104.1), turned to 270 degrees
- moved R21 57.8 mm to (131.6, 95.4), turned to 180 degrees
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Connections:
- C14 pad 2: /Power Supply/VCC_SEC_ELM -> /Peripherals/VCC_SENSORS
- C15 pad 2: /Power Supply/VCC_SEC_ELM -> /Peripherals/VCC_SENSORS
- C17 pad 2: /Power Supply/VCC_SEC_ELM -> /Peripherals/VCC_SENSORS
- C19 pad 2: /Power Supply/VCC_SEC_ELM -> /Peripherals/VCC_SENSORS
- D2 pad 2: Net-(D2-Pad2) -> (no net)
- J1 pad 1: Net-(J1-Pad1) -> /LoRa MCU/I2C1_SDA
- J1 pad 2: Net-(J1-Pad2) -> /LoRa MCU/I2C1_SCL
- JP1 pad 2: /Peripherals/VCC_SEC_ELM -> /Peripherals/VCC_SENSORS
- JP3 pad 2: /Power Supply/VCC_SEC_ELM -> /Peripherals/VCC_SEC_ELM
- JP9 pad 3: /Peripherals/LED_G -> /Peripherals/ACCEL_INT1
- R1 pad 2: /LoRa MCU/PB7 -> /LoRa MCU/PB12
- R11 pad 2: Net-(R11-Pad2) -> /Peripherals/FlashCS
- R12 pad 2: /Power Supply/VCC_SEC_ELM -> /Peripherals/VCC_SENSORS
- R13 pad 1: /Power Supply/VCC_SEC_ELM -> /Peripherals/VCC_SENSORS
- R18 pad 1: Net-(D2-Pad2) -> Net-(AE1-Pad1)
- R18 pad 2: /Peripherals/LED_G -> Net-(C57-Pad2)
- R3 pad 1: /Peripherals/VCC_SEC_ELM -> /Peripherals/VCC_SENSORS
- R4 pad 2: /LoRa MCU/PB5 -> /LoRa MCU/PB7
- R8 pad 1: /Power Supply/VCC_SEC_ELM -> /Peripherals/VCC_SEC_ELM
- U1 pad 3: /LoRa MCU/PB7 -> /LoRa MCU/PB12
- U1 pad 6: /Peripherals/VCC_SEC_ELM -> /Peripherals/VCC_SENSORS
- U3 pad 3: /LoRa MCU/PB5 -> /LoRa MCU/PB7
- U4 pad 6: /Power Supply/VCC_SEC_ELM -> /Peripherals/VCC_SEC_ELM
- U5 pad 1: Net-(R11-Pad2) -> /Peripherals/FlashCS
- U6 pad 10: /Power Supply/VCC_SEC_ELM -> /Peripherals/VCC_SENSORS
- U6 pad 2: /Power Supply/VCC_SEC_ELM -> /Peripherals/VCC_SENSORS
- U6 pad 3: /Power Supply/VCC_SEC_ELM -> /Peripherals/VCC_SENSORS
- U6 pad 9: /Power Supply/VCC_SEC_ELM -> /Peripherals/VCC_SENSORS
- U7 pad 1: /Power Supply/VCC_SEC_ELM -> /Peripherals/VCC_SENSORS
- U9 pad 16: /Peripherals/ACCEL_INT1 -> Net-(JP9-Pad2)
- U9 pad 3: /LoRa MCU/PB5 -> /Peripherals/LED_B
- U9 pad 32: Net-(JP9-Pad2) -> /LoRa MCU/PB12
- U9 pad 6: /Peripherals/LED_B -> /Peripherals/FlashCS
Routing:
- net Net-(BH2-Pad1): track 0.00 -> 30.5 mm
- net VDD: track 0.00 -> 28.6 mm, vias 0 -> 12
- net Net-(BH1-Pad1): track 0.00 -> 21.0 mm
- net +BATT: track 0.00 -> 15.0 mm
- net GND: track 0.00 -> 14.4 mm, vias 0 -> 23
- net Net-(C10-Pad2): track 0.00 -> 6.44 mm
- net VDDA: track 0.00 -> 4.93 mm
- net Net-(L1-Pad2): track 0.00 -> 3.64 mm
- net Net-(L1-Pad1): track 0.00 -> 3.55 mm
- net Net-(C1-Pad2): track 0.00 -> 3.48 mm
- net /LoRa MCU/PB4: track 0.00 -> 1.53 mm
- net VDDRF1V55: track 0.00 -> 1.43 mm
- net VLXSMPS: track 0.00 -> 0.95 mm
- added copper zone on F.Cu, net +BATT
- added copper zone on B.Cu, net GND
- added copper zone on F.Cu, net GND
- added copper zone on In1.GND, net GND
- added copper zone on F.Cu, net Net-(BH1-Pad1)
- added copper zone on F.Cu, net Net-(C10-Pad2)
- added copper zone on F.Cu, net Net-(L1-Pad1)
- added copper zone on F.Cu, net Net-(L1-Pad2)
- added copper zone on F.Cu, net VDD
- added copper zone on In2.PWR, net VDD
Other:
- outline, holes or cut-outs redrawn
- copper layers 2 -> 4
- net class Default: clearance 0.2 -> 0.1524; trace_width 0.25 -> 0.1524
- rule trace_clearance: 0.2 -> 0.1524
- rule trace_min: 0.2 -> 0.127
- rule via_min_drill: 0.3 -> 0.2
- rule via_min_size: 0.4 -> 0.45
- board text added: "+"
- board text added: "-"
- board text added: "Accelerometer"
- board text added: "BOOT0"
- board text added: "Flash Memory"
- board text added: "Generic Node"
- board text added: "RESET"
- board text added: "Secure Element"
- board text added: "Temperature Humidity Sensor"
- board text added: "USR BTN"
